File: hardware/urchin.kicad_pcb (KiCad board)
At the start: 2 copper layers, 20 parts, among them IC1 ATMEGA328PB-A, IC2 ATTINY85-S, P1 CONN_02X03, P2 USB_OTG, U1 CH340G, Y1 12M

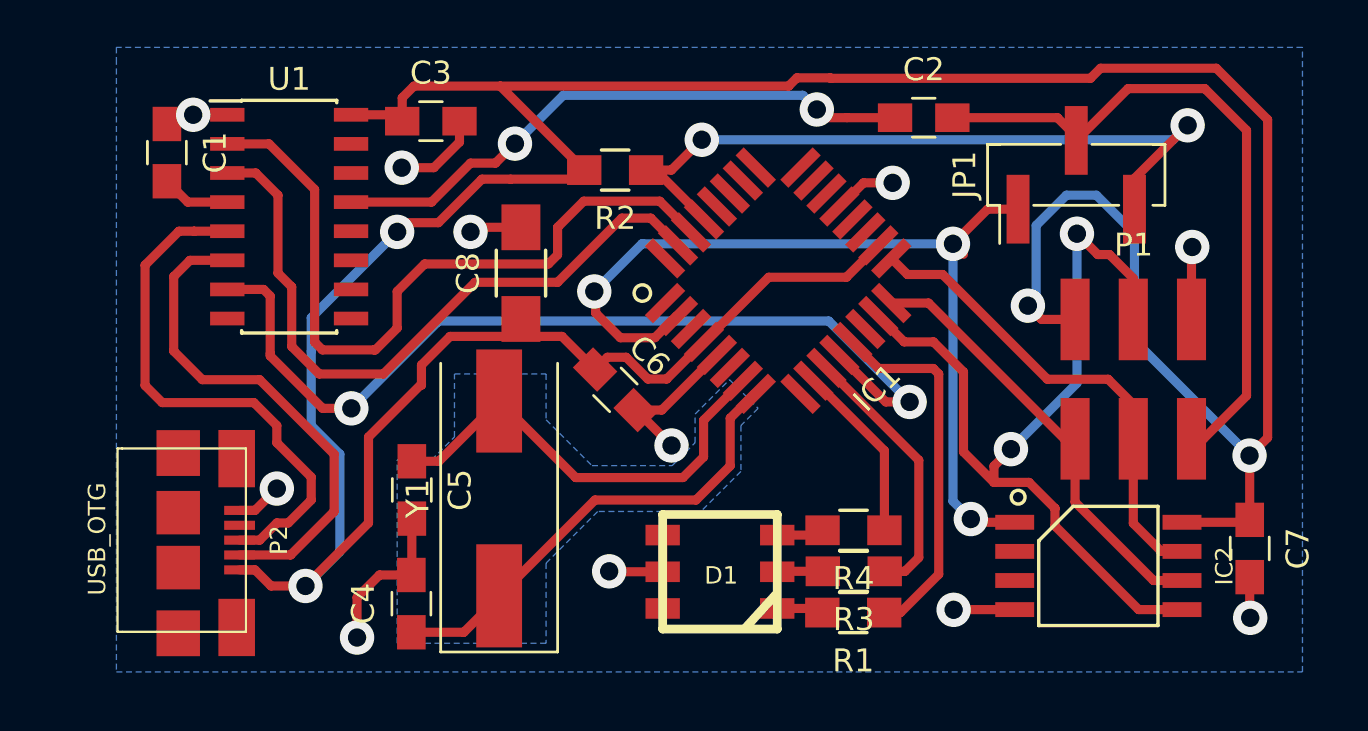
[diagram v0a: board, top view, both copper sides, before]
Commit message: Updating schematic to include name/date; minor changes.
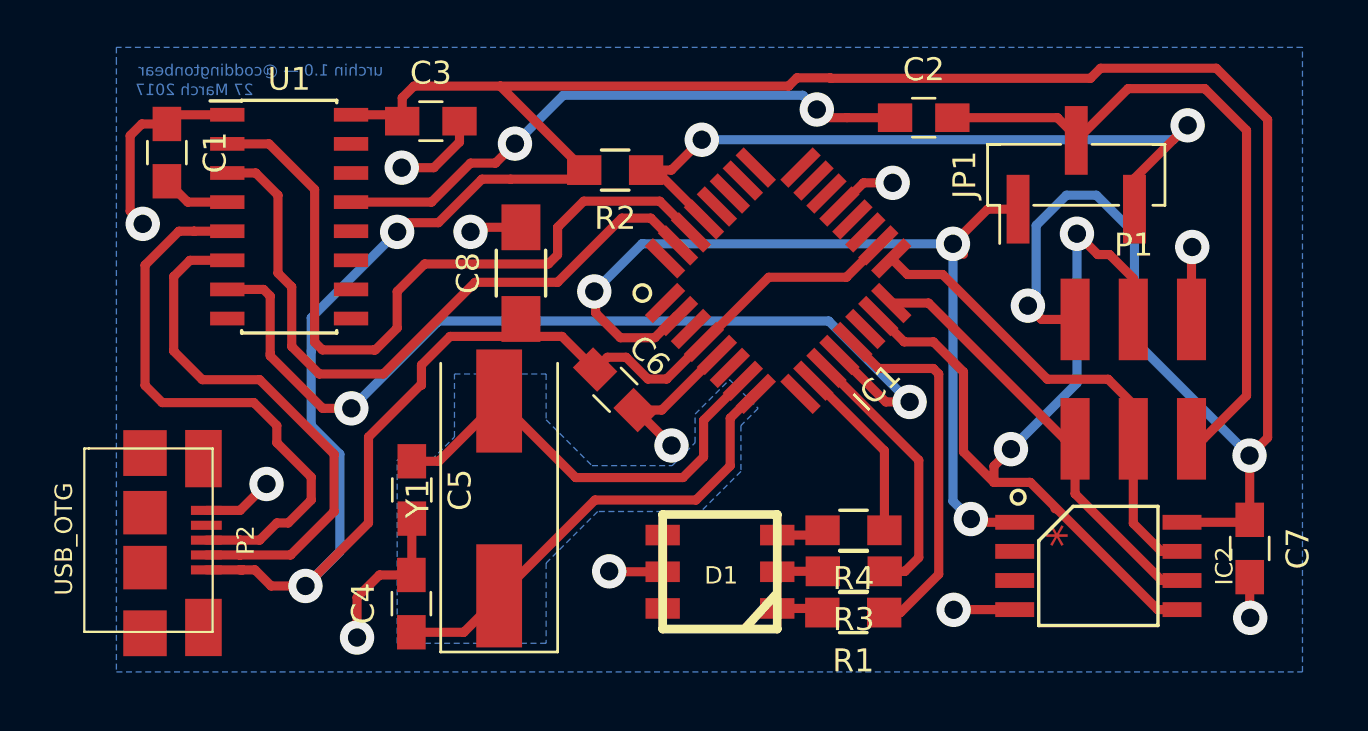
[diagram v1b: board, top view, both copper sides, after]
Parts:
- moved P2 1.45 mm to (110.5, 108.8)
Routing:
- net GND: track 41.1 -> 48.7 mm
- net +5V: track 158.3 -> 159.9 mm
- net Net-(P2-Pad3): track 23.6 -> 25.1 mm
- net Net-(P2-Pad2): track 22.2 -> 23.6 mm
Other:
- net class Default: clearance 0.3 -> 0.17
- rule trace_clearance: 0.3 -> 0.17
- board text added: "*"
- board text added: "27 March 2017"
- board text added: "urchin 1.0 — @coddingtonbear"

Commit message: Updating to latest hardware file.
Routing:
- net GND: track 48.7 -> 94.8 mm, vias 11 -> 8
- net Net-(P2-Pad3): track 25.1 -> 24.5 mm
